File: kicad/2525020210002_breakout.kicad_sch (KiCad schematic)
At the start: 13 parts, among them J1 I2C_IN, J2 I2C_OUT, J3 Conn_01x04_Socket, U1 2525020210002

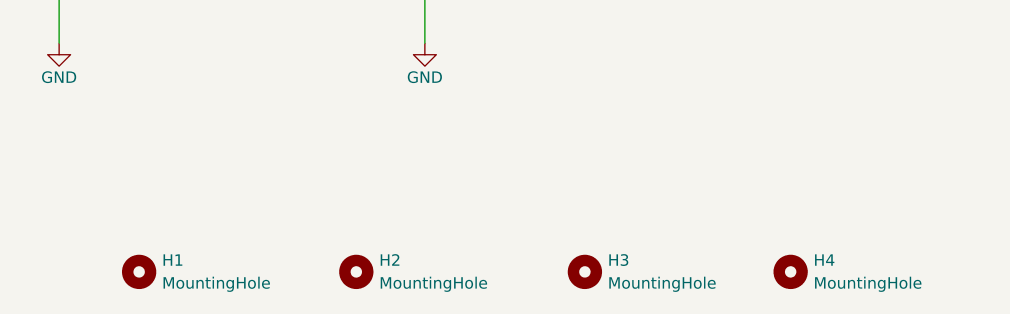
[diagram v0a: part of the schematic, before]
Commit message: README.md update, schematic m.hole sz lbl
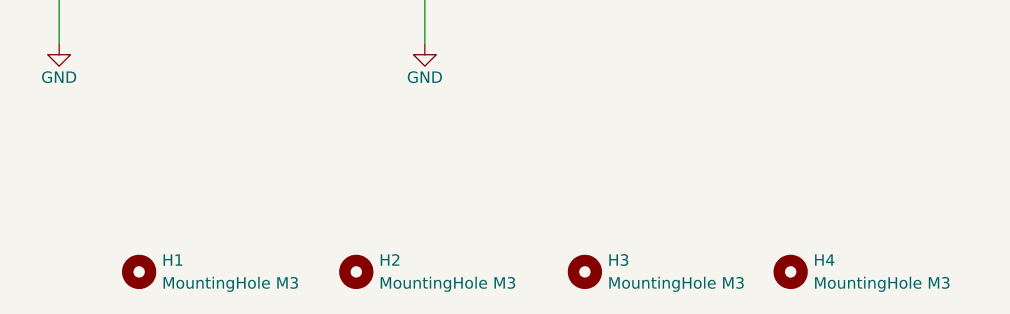
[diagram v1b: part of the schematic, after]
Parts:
- H1, H2, H3, H4: value MountingHole -> MountingHole M3
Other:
- moved on the sheet: H2
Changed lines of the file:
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@@
         )
       )
-      (project "BiltongBoardSensorExpansion"
+      (project "2525020210002_breakout"
         (path "/0ecd3e45-e5d3-482a-bb8f-58facd05184d"
           (reference "R1") (unit 1)
@@
     (pin "4")
     (instances
-      (project "BiltongBoardSensorExpansion"
+      (project "2525020210002_breakout"
         (path "/0ecd3e45-e5d3-482a-bb8f-58facd05184d"
           (reference "J1") (unit 1)
@@
         )
       )
-      (project "BiltongBoardSensorExpansion"
+      (project "2525020210002_breakout"
         (path "/0ecd3e45-e5d3-482a-bb8f-58facd05184d"
           (reference "#PWR01") (unit 1)
@@
         )
       )
-      (project "BiltongBoardSensorExpansion"
+      (project "2525020210002_breakout"
         (path "/0ecd3e45-e5d3-482a-bb8f-58facd05184d"
           (reference "#PWR04") (unit 1)
@@
     (pin "4")
     (instances
-      (project "BiltongBoardSensorExpansion"
+      (project "2525020210002_breakout"
         (path "/0ecd3e45-e5d3-482a-bb8f-58facd05184d"
           (reference "J2") (unit 1)
@@
         )
       )
-      (project "BiltongBoardSensorExpansion"
+      (project "2525020210002_breakout"
         (path "/0ecd3e45-e5d3-482a-bb8f-58facd05184d"
           (reference "#PWR07") (unit 1)
@@
       (effects (font (size 1.27 1.27)) (justify left))
     )
-    (property "Value" "MountingHole" (at 264.16 138.43 0)
+    (property "Value" "MountingHole M3" (at 264.16 138.43 0)
       (effects (font (size 1.27 1.27)) (justify left))
     )
@@
     )
     (instances
-      (project "BiltongBoardSensorExpansion"
+      (project "2525020210002_breakout"
         (path "/0ecd3e45-e5d3-482a-bb8f-58facd05184d"
           (reference "H4") (unit 1)
@@
     (pin "2")
     (instances
-      (project "BiltongBoardSensorExpansion"
+      (project "2525020210002_breakout"
         (path "/0ecd3e45-e5d3-482a-bb8f-58facd05184d"
           (reference "D1") (unit 1)
@@
         )
       )
-      (project "BiltongBoardSensorExpansion"
+      (project "2525020210002_breakout"
         (path "/0ecd3e45-e5d3-482a-bb8f-58facd05184d"
           (reference "#PWR03") (unit 1)
@@
         )
       )
-      (project "BiltongBoardSensorExpansion"
+      (project "2525020210002_breakout"
         (path "/0ecd3e45-e5d3-482a-bb8f-58facd05184d"
           (reference "#PWR012") (unit 1)
@@
         )
       )
-      (project "BiltongBoardSensorExpansion"
+      (project "2525020210002_breakout"
         (path "/0ecd3e45-e5d3-482a-bb8f-58facd05184d"
           (reference "#PWR09") (unit 1)
@@
         )
       )
-      (project "BiltongBoardSensorExpansion"
+      (project "2525020210002_breakout"
         (path "/0ecd3e45-e5d3-482a-bb8f-58facd05184d"
           (reference "R2") (unit 1)
@@
         )
       )
-      (project "BiltongBoardSensorExpansion"
+      (project "2525020210002_breakout"
         (path "/0ecd3e45-e5d3-482a-bb8f-58facd05184d"
           (reference "#PWR02") (unit 1)
@@
         )
       )
-      (project "BiltongBoardSensorExpansion"
+      (project "2525020210002_breakout"
         (path "/0ecd3e45-e5d3-482a-bb8f-58facd05184d"
           (reference "C1") (unit 1)
@@
     )
   )
-  (symbol (lib_id "Mechanical:MountingHole") (at 213.36 137.16 0) (unit 1)
-    (in_bom yes) (on_board yes) (dnp no) (fields_autoplaced)
-    (property "Reference" "H2" (at 215.9 135.89 0)
-      (effects (font (size 1.27 1.27)) (justify left))
-    )
-    (property "Value" "MountingHole" (at 215.9 138.43 0)
-      (effects (font (size 1.27 1.27)) (justify left))
+  (symbol (lib_id "Mechanical:MountingHole") (at 213.36 137.16 90) (unit 1)
+    (in_bom yes) (on_board yes) (dnp no) (fields_autoplaced)
+    (property "Reference" "H2" (at 215.9 135.89 90)
+      (effects (font (size 1.27 1.27)) (justify right))
+    )
+    (property "Value" "MountingHole M3" (at 215.9 138.43 90)
+      (effects (font (size 1.27 1.27)) (justify right))
     )
     (property "Footprint" "MountingHole:MountingHole_3.2mm_M3" (at 213.36 137.16 0)
@@
     )
     (instances
-      (project "BiltongBoardSensorExpansion"
+      (project "2525020210002_breakout"
         (path "/0ecd3e45-e5d3-482a-bb8f-58facd05184d"
           (reference "H2") (unit 1)
@@
     (pin "4")
     (instances
-      (project "BiltongBoardSensorExpansion"
+      (project "2525020210002_breakout"
         (path "/0ecd3e45-e5d3-482a-bb8f-58facd05184d"
           (reference "J3") (unit 1)
@@
         )
       )
-      (project "BiltongBoardSensorExpansion"
+      (project "2525020210002_breakout"
         (path "/0ecd3e45-e5d3-482a-bb8f-58facd05184d"
           (reference "#PWR010") (unit 1)
@@
   )
   (symbol (lib_id "Mechanical:MountingHole") (at 238.76 137.16 0) (unit 1)
-    (in_bom yes) (on_board yes) (dnp no) (fields_autoplaced)
+    (in_bom yes) (on_board yes) (dnp no)
     (property "Reference" "H3" (at 241.3 135.89 0)
       (effects (font (size 1.27 1.27)) (justify left))
     )
-    (property "Value" "MountingHole" (at 241.3 138.43 0)
+    (property "Value" "MountingHole M3" (at 241.3 138.43 0)
       (effects (font (size 1.27 1.27)) (justify left))
     )
@@
     )
     (instances
-      (project "BiltongBoardSensorExpansion"
+      (project "2525020210002_breakout"
         (path "/0ecd3e45-e5d3-482a-bb8f-58facd05184d"
           (reference "H3") (unit 1)
@@
         )
       )
-      (project "BiltongBoardSensorExpansion"
+      (project "2525020210002_breakout"
         (path "/0ecd3e45-e5d3-482a-bb8f-58facd05184d"
           (reference "#PWR05") (unit 1)
@@
       (effects (font (size 1.27 1.27)) (justify left))
     )
-    (property "Value" "MountingHole" (at 191.77 138.43 0)
+    (property "Value" "MountingHole M3" (at 191.77 138.43 0)
       (effects (font (size 1.27 1.27)) (justify left))
     )
@@
     )
     (instances
-      (project "BiltongBoardSensorExpansion"
+      (project "2525020210002_breakout"
         (path "/0ecd3e45-e5d3-482a-bb8f-58facd05184d"
           (reference "H1") (unit 1)
@@
         )
       )
-      (project "BiltongBoardSensorExpansion"
+      (project "2525020210002_breakout"
         (path "/0ecd3e45-e5d3-482a-bb8f-58facd05184d"
           (reference "#PWR011") (unit 1)
@@
         )
       )
-      (project "BiltongBoardSensorExpansion"
+      (project "2525020210002_breakout"
         (path "/0ecd3e45-e5d3-482a-bb8f-58facd05184d"
           (reference "R3") (unit 1)
@@
         )
       )
-      (project "BiltongBoardSensorExpansion"
+      (project "2525020210002_breakout"
         (path "/0ecd3e45-e5d3-482a-bb8f-58facd05184d"
           (reference "#PWR06") (unit 1)
@@
     (pin "4")
     (instances
-      (project "BiltongBoardSensorExpansion"
+      (project "2525020210002_breakout"
         (path "/0ecd3e45-e5d3-482a-bb8f-58facd05184d"
           (reference "U1") (unit 1)
@@
         )
       )
-      (project "BiltongBoardSensorExpansion"
+      (project "2525020210002_breakout"
         (path "/0ecd3e45-e5d3-482a-bb8f-58facd05184d"
           (reference "#PWR08") (unit 1)

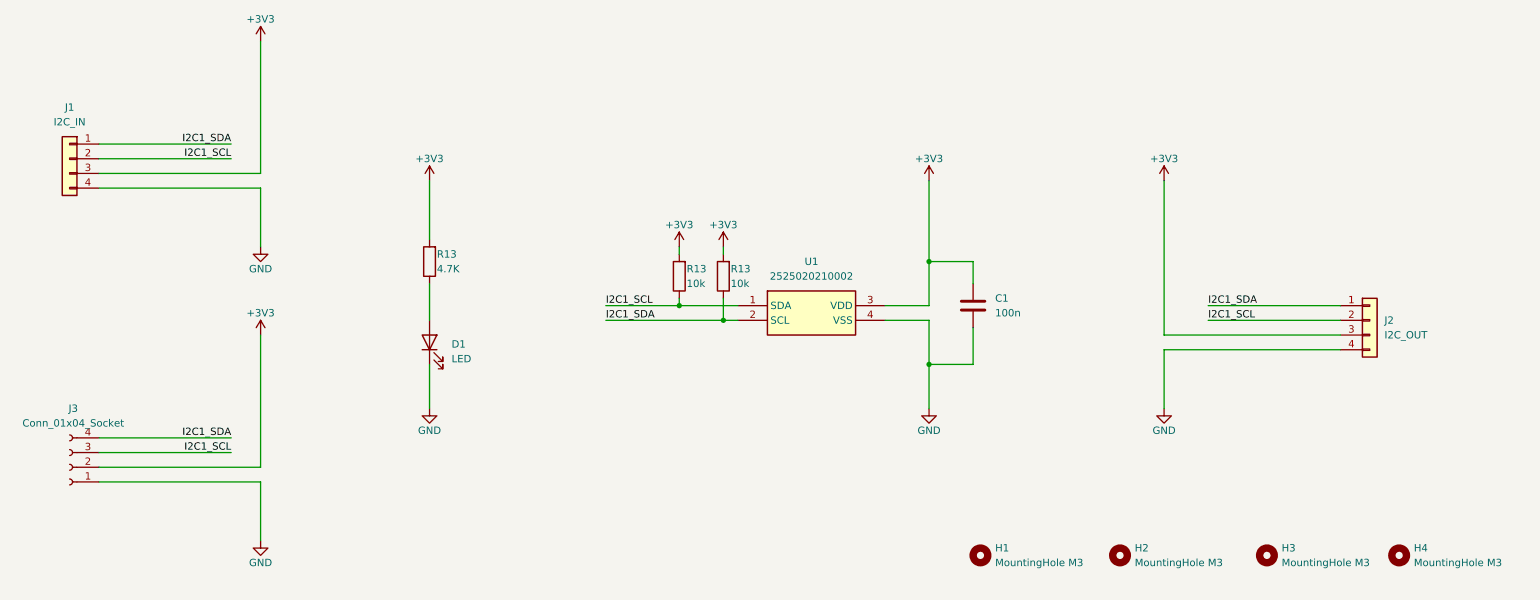
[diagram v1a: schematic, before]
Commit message: generated BOM, fixed fab layer error
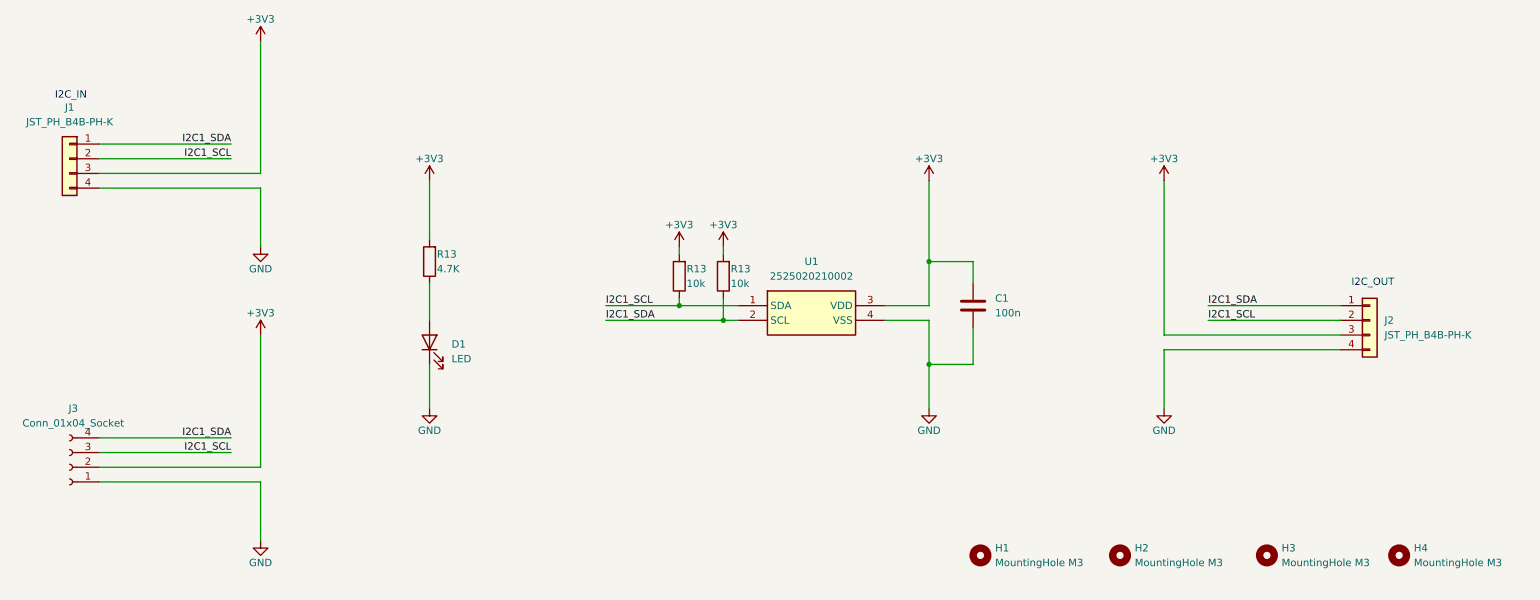
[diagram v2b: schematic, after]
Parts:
- H1, H2, H3, H4: now left out of the parts list
- J1: value I2C_IN -> JST_PH_B4B-PH-K
- J2: value I2C_OUT -> JST_PH_B4B-PH-K
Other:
- note added: "I2C_IN"
- note added: "I2C_OUT"
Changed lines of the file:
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@@
     (stroke (width 0) (type default))
+  )
+  (text "I2C_OUT" (at 253.365 90.805 0)
+    (effects (font (size 1.27 1.27)) (justify left bottom))
+  )
+  (text "I2C_IN" (at 29.21 58.42 0)
+    (effects (font (size 1.27 1.27)) (justify left bottom))
   )
   (label "I2C1_SDA" (at 59.69 66.04 180) (fields_autoplaced)
@@
       (effects (font (size 1.27 1.27)))
     )
-    (property "Value" "I2C_IN" (at 31.75 62.23 0)
+    (property "Value" "JST_PH_B4B-PH-K" (at 31.75 62.23 0)
       (effects (font (size 1.27 1.27)))
     )
@@
   )
   (symbol (lib_id "Connector_Generic:Conn_01x04") (at 256.54 96.52 0) (unit 1)
-    (in_bom yes) (on_board yes) (dnp no) (fields_autoplaced)
+    (in_bom yes) (on_board yes) (dnp no)
     (property "Reference" "J2" (at 259.08 96.52 0)
       (effects (font (size 1.27 1.27)) (justify left))
     )
-    (property "Value" "I2C_OUT" (at 259.08 99.06 0)
+    (property "Value" "JST_PH_B4B-PH-K" (at 259.08 99.06 0)
       (effects (font (size 1.27 1.27)) (justify left))
     )
@@
   )
   (symbol (lib_id "Mechanical:MountingHole") (at 261.62 137.16 0) (unit 1)
-    (in_bom yes) (on_board yes) (dnp no) (fields_autoplaced)
+    (in_bom no) (on_board yes) (dnp no) (fields_autoplaced)
     (property "Reference" "H4" (at 264.16 135.89 0)
       (effects (font (size 1.27 1.27)) (justify left))
@@
   )
   (symbol (lib_id "Mechanical:MountingHole") (at 213.36 137.16 90) (unit 1)
-    (in_bom yes) (on_board yes) (dnp no) (fields_autoplaced)
+    (in_bom no) (on_board yes) (dnp no) (fields_autoplaced)
     (property "Reference" "H2" (at 215.9 135.89 90)
       (effects (font (size 1.27 1.27)) (justify right))
@@
   )
   (symbol (lib_id "Mechanical:MountingHole") (at 238.76 137.16 0) (unit 1)
-    (in_bom yes) (on_board yes) (dnp no)
+    (in_bom no) (on_board yes) (dnp no)
     (property "Reference" "H3" (at 241.3 135.89 0)
       (effects (font (size 1.27 1.27)) (justify left))
@@
   )
   (symbol (lib_id "Mechanical:MountingHole") (at 189.23 137.16 0) (unit 1)
-    (in_bom yes) (on_board yes) (dnp no) (fields_autoplaced)
+    (in_bom no) (on_board yes) (dnp no) (fields_autoplaced)
     (property "Reference" "H1" (at 191.77 135.89 0)
       (effects (font (size 1.27 1.27)) (justify left))

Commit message: missing LED part no.
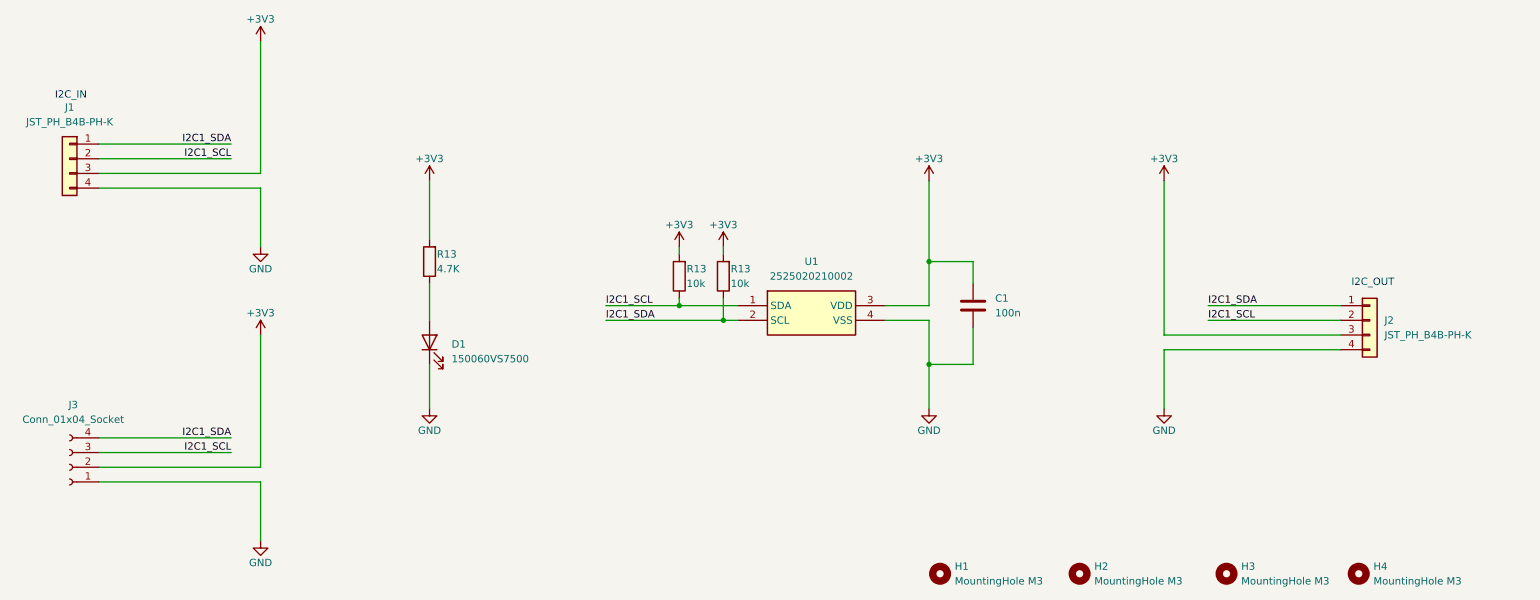
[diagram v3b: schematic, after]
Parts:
- D1: value LED -> 150060VS7500
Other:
- moved on the sheet: H1, H2, H3, H4
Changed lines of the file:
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@@
     )
   )
-  (symbol (lib_id "Mechanical:MountingHole") (at 261.62 137.16 0) (unit 1)
+  (symbol (lib_id "Mechanical:MountingHole") (at 254.635 140.335 0) (unit 1)
     (in_bom no) (on_board yes) (dnp no) (fields_autoplaced)
-    (property "Reference" "H4" (at 264.16 135.89 0)
-      (effects (font (size 1.27 1.27)) (justify left))
-    )
-    (property "Value" "MountingHole M3" (at 264.16 138.43 0)
-      (effects (font (size 1.27 1.27)) (justify left))
-    )
-    (property "Footprint" "MountingHole:MountingHole_3.2mm_M3" (at 261.62 137.16 0)
-      (effects (font (size 1.27 1.27)) hide)
-    )
-    (property "Datasheet" "~" (at 261.62 137.16 0)
+    (property "Reference" "H4" (at 257.175 139.065 0)
+      (effects (font (size 1.27 1.27)) (justify left))
+    )
+    (property "Value" "MountingHole M3" (at 257.175 141.605 0)
+      (effects (font (size 1.27 1.27)) (justify left))
+    )
+    (property "Footprint" "MountingHole:MountingHole_3.2mm_M3" (at 254.635 140.335 0)
+      (effects (font (size 1.27 1.27)) hide)
+    )
+    (property "Datasheet" "~" (at 254.635 140.335 0)
       (effects (font (size 1.27 1.27)) hide)
     )
@@
       (effects (font (size 1.27 1.27)) (justify right))
     )
-    (property "Value" "LED" (at 97.79 103.1875 90)
+    (property "Value" "150060VS7500" (at 97.79 103.1875 90)
       (effects (font (size 1.27 1.27)) (justify right))
     )
@@
       (effects (font (size 1.27 1.27)) hide)
     )
-    (property "Datasheet" "~" (at 93.98 100.33 0)
+    (property "Datasheet" "https://www.digikey.com/en/products/detail/w%C3%BCrth-elektronik/150060VS75000/4489906" (at 93.98 100.33 0)
       (effects (font (size 1.27 1.27)) hide)
     )
@@
     )
   )
-  (symbol (lib_id "Mechanical:MountingHole") (at 213.36 137.16 90) (unit 1)
+  (symbol (lib_id "Mechanical:MountingHole") (at 206.375 140.335 90) (unit 1)
     (in_bom no) (on_board yes) (dnp no) (fields_autoplaced)
-    (property "Reference" "H2" (at 215.9 135.89 90)
-      (effects (font (size 1.27 1.27)) (justify right))
-    )
-    (property "Value" "MountingHole M3" (at 215.9 138.43 90)
-      (effects (font (size 1.27 1.27)) (justify right))
-    )
-    (property "Footprint" "MountingHole:MountingHole_3.2mm_M3" (at 213.36 137.16 0)
-      (effects (font (size 1.27 1.27)) hide)
-    )
-    (property "Datasheet" "~" (at 213.36 137.16 0)
+    (property "Reference" "H2" (at 208.915 139.065 90)
+      (effects (font (size 1.27 1.27)) (justify right))
+    )
+    (property "Value" "MountingHole M3" (at 208.915 141.605 90)
+      (effects (font (size 1.27 1.27)) (justify right))
+    )
+    (property "Footprint" "MountingHole:MountingHole_3.2mm_M3" (at 206.375 140.335 0)
+      (effects (font (size 1.27 1.27)) hide)
+    )
+    (property "Datasheet" "~" (at 206.375 140.335 0)
       (effects (font (size 1.27 1.27)) hide)
     )
@@
   )
   (symbol (lib_id "Connector:Conn_01x04_Socket") (at 31.75 121.92 180) (unit 1)
-    (in_bom yes) (on_board yes) (dnp no) (fields_autoplaced)
-    (property "Reference" "J3" (at 32.385 111.76 0)
-      (effects (font (size 1.27 1.27)))
-    )
-    (property "Value" "Conn_01x04_Socket" (at 32.385 114.3 0)
+    (in_bom yes) (on_board yes) (dnp no)
+    (property "Reference" "J3" (at 32.385 111.125 0)
+      (effects (font (size 1.27 1.27)))
+    )
+    (property "Value" "Conn_01x04_Socket" (at 32.385 113.665 0)
       (effects (font (size 1.27 1.27)))
     )
@@
     )
   )
-  (symbol (lib_id "Mechanical:MountingHole") (at 238.76 137.16 0) (unit 1)
+  (symbol (lib_id "Mechanical:MountingHole") (at 231.775 140.335 0) (unit 1)
     (in_bom no) (on_board yes) (dnp no)
-    (property "Reference" "H3" (at 241.3 135.89 0)
-      (effects (font (size 1.27 1.27)) (justify left))
-    )
-    (property "Value" "MountingHole M3" (at 241.3 138.43 0)
-      (effects (font (size 1.27 1.27)) (justify left))
-    )
-    (property "Footprint" "MountingHole:MountingHole_3.2mm_M3" (at 238.76 137.16 0)
-      (effects (font (size 1.27 1.27)) hide)
-    )
-    (property "Datasheet" "~" (at 238.76 137.16 0)
+    (property "Reference" "H3" (at 234.315 139.065 0)
+      (effects (font (size 1.27 1.27)) (justify left))
+    )
+    (property "Value" "MountingHole M3" (at 234.315 141.605 0)
+      (effects (font (size 1.27 1.27)) (justify left))
+    )
+    (property "Footprint" "MountingHole:MountingHole_3.2mm_M3" (at 231.775 140.335 0)
+      (effects (font (size 1.27 1.27)) hide)
+    )
+    (property "Datasheet" "~" (at 231.775 140.335 0)
       (effects (font (size 1.27 1.27)) hide)
     )
@@
     )
   )
-  (symbol (lib_id "Mechanical:MountingHole") (at 189.23 137.16 0) (unit 1)
+  (symbol (lib_id "Mechanical:MountingHole") (at 182.245 140.335 0) (unit 1)
     (in_bom no) (on_board yes) (dnp no) (fields_autoplaced)
-    (property "Reference" "H1" (at 191.77 135.89 0)
-      (effects (font (size 1.27 1.27)) (justify left))
-    )
-    (property "Value" "MountingHole M3" (at 191.77 138.43 0)
-      (effects (font (size 1.27 1.27)) (justify left))
-    )
-    (property "Footprint" "MountingHole:MountingHole_3.2mm_M3" (at 189.23 137.16 0)
-      (effects (font (size 1.27 1.27)) hide)
-    )
-    (property "Datasheet" "~" (at 189.23 137.16 0)
-      (effects (font (size 1.27 1.27)) hide)
-    )
+    (property "Reference" "H1" (at 184.785 139.065 0)
+      (effects (font (size 1.27 1.27)) (justify left))
+    )
+    (property "Value" "MountingHole M3" (at 184.785 141.605 0)
+      (effects (font (size 1.27 1.27)) (justify left))
+    )
+    (property "Footprint" "MountingHole:MountingHole_3.2mm_M3" (at 182.245 140.335 0)
+      (effects (font (size 1.27 1.27)) hide)
+    )
+    (property "Datasheet" "~" (at 182.245 140.335 0)
+      (effects (font (size 1.27 1.27)) hide)
+    )
